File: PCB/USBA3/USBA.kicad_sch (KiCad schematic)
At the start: 22 parts, among them J1 USB_A, U1 ESP32-PICO-MINI-02, U2 Barcode, U3 CH340X, U4 QR, U5 MD8942

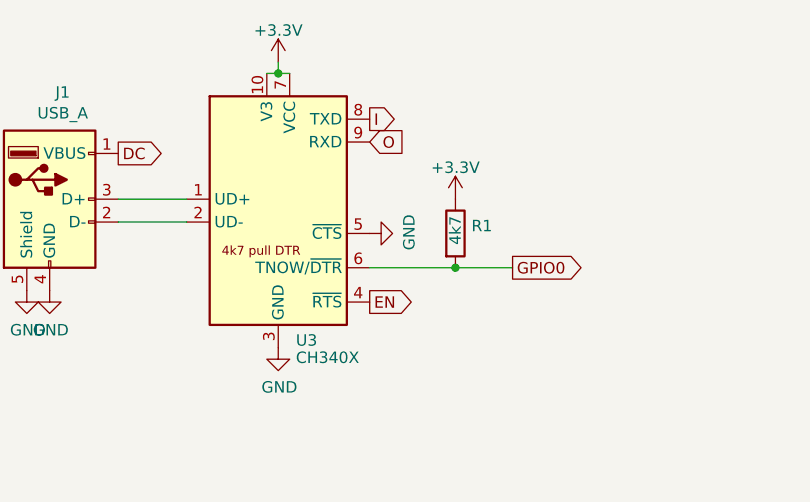
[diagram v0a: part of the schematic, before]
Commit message: Fix CH340X
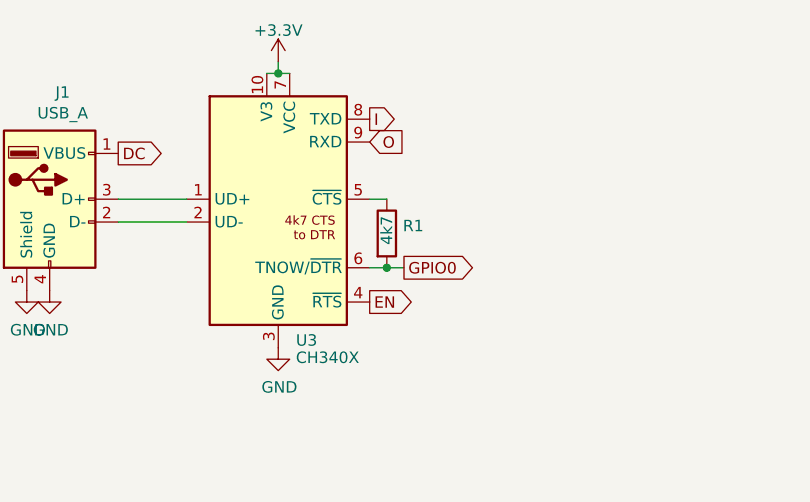
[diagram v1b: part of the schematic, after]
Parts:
- U3: JLCPCB Rotation Offset -90 -> 90
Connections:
- net +3.3V: no longer R1.1
- net GND: no longer U3.5 (~{CTS})
- new net: R1.1, U3.5 (~{CTS})
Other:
- moved on the sheet: R1
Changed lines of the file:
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@@
   (junction (at 193.04 43.18) (diameter 0) (color 0 0 0 0)
   )
-  (junction (at 212.725 64.77) (diameter 0) (color 0 0 0 0)
+  (junction (at 205.105 64.77) (diameter 0) (color 0 0 0 0)
   )
   (junction (at 78.74 49.53) (diameter 0) (color 0 0 0 0)
@@
     (stroke (width 0) (type default))
   )
-  (wire (pts (xy 203.2 64.77) (xy 212.725 64.77))
+  (wire (pts (xy 203.2 64.77) (xy 205.105 64.77))
     (stroke (width 0) (type default))
   )
@@
     (stroke (width 0) (type default))
   )
-  (wire (pts (xy 212.725 64.77) (xy 219.075 64.77))
+  (wire (pts (xy 205.105 64.77) (xy 207.01 64.77))
     (stroke (width 0) (type default))
   )
@@
   )
   (wire (pts (xy 193.04 41.91) (xy 193.04 43.18))
+    (stroke (width 0) (type default))
+  )
+  (wire (pts (xy 203.2 57.15) (xy 205.105 57.15))
     (stroke (width 0) (type default))
   )
@@
     )
   )
-  (global_label "GPIO0" (shape output) (at 219.075 64.77 0) (fields_autoplaced)
-    (effects (font (size 1.27 1.27)) (justify left))
-    (property "Intersheetrefs" "${INTERSHEET_REFS}" (at 227.0114 64.77 0)
+  (global_label "GPIO0" (shape output) (at 207.01 64.77 0) (fields_autoplaced)
+    (effects (font (size 1.27 1.27)) (justify left))
+    (property "Intersheetrefs" "${INTERSHEET_REFS}" (at 214.9464 64.77 0)
       (effects (font (size 1.27 1.27)) (justify left) hide)
     )
@@
       (effects (font (size 1.27 1.27)) hide)
     )
-    (property "JLCPCB Rotation Offset" "-90" (at 203.2 54.61 0)
+    (property "JLCPCB Rotation Offset" "90" (at 203.2 54.61 0)
       (effects (font (size 1.27 1.27)) hide)
     )
@@
     )
   )
-  (symbol (lib_id "Device:R") (at 212.725 60.96 0) (unit 1)
-    (in_bom yes) (on_board yes) (dnp no)
-    (property "Reference" "R1" (at 214.503 60.1253 0)
-      (effects (font (size 1.27 1.27)) (justify left))
-    )
-    (property "Value" "4k7" (at 212.725 62.23 90)
-      (effects (font (size 1.27 1.27)) (justify left))
-    )
-    (property "Footprint" "RevK:R_0402" (at 210.947 60.96 90)
-      (effects (font (size 1.27 1.27)) hide)
-    )
-    (property "Datasheet" "~" (at 212.725 60.96 0)
+  (symbol (lib_id "Device:R") (at 205.105 60.96 0) (unit 1)
+    (in_bom yes) (on_board yes) (dnp no)
+    (property "Reference" "R1" (at 206.883 60.1253 0)
+      (effects (font (size 1.27 1.27)) (justify left))
+    )
+    (property "Value" "4k7" (at 205.105 62.23 90)
+      (effects (font (size 1.27 1.27)) (justify left))
+    )
+    (property "Footprint" "RevK:R_0402" (at 203.327 60.96 90)
+      (effects (font (size 1.27 1.27)) hide)
+    )
+    (property "Datasheet" "~" (at 205.105 60.96 0)
       (effects (font (size 1.27 1.27)) hide)
     )
@@
     )
   )
-  (symbol (lib_id "power:GND") (at 203.2 60.96 90) (unit 1)
-    (in_bom yes) (on_board yes) (dnp no)
-    (property "Reference" "#PWR02" (at 209.55 60.96 0)
-      (effects (font (size 1.27 1.27)) hide)
-    )
-    (property "Value" "GND" (at 207.5942 60.833 0)
-      (effects (font (size 1.27 1.27)))
-    )
-    (property "Footprint" "" (at 203.2 60.96 0)
-      (effects (font (size 1.27 1.27)) hide)
-    )
-    (property "Datasheet" "" (at 203.2 60.96 0)
-      (effects (font (size 1.27 1.27)) hide)
-    )
-    (pin "1")
-    (instances
-      (project "USBA"
-        (path "/2d210a96-f81f-42a9-8bf4-1b43c11086f3"
-          (reference "#PWR02") (unit 1)
-        )
-      )
-    )
-  )
   (symbol (lib_id "RevK:PCB") (at 250.19 172.72 0) (unit 1)
     (in_bom no) (on_board yes) (dnp no)
@@
         )
       )
-    )
-  )
-  (symbol (lib_id "power:+3.3V") (at 212.725 57.15 0) (unit 1)
-    (in_bom yes) (on_board yes) (dnp no) (fields_autoplaced)
-    (property "Reference" "#PWR05" (at 212.725 60.96 0)
-      (effects (font (size 1.27 1.27)) hide)
-    )
-    (property "Value" "+3.3V" (at 212.725 53.6481 0)
-      (effects (font (size 1.27 1.27)))
-    )
-    (property "Footprint" "" (at 212.725 57.15 0)
-      (effects (font (size 1.27 1.27)) hide)
-    )
-    (property "Datasheet" "" (at 212.725 57.15 0)
-      (effects (font (size 1.27 1.27)) hide)
-    )
-    (pin "1")
-    (instances
-      (project "USBA"
-        (path "/2d210a96-f81f-42a9-8bf4-1b43c11086f3"
-          (reference "#PWR05") (unit 1)
-        )
-      )

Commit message: Tidy
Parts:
- removed C5: 1uF, RevK:C_0402, symbol Device:C
- removed R1: 4k7, RevK:R_0402, symbol Device:R
- removed R6: 10k, RevK:R_0402, symbol Device:R
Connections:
- net GPIO0: now also U3.5 (~{CTS})
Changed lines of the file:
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@@
   (junction (at 193.04 43.18) (diameter 0) (color 0 0 0 0)
   )
-  (junction (at 205.105 64.77) (diameter 0) (color 0 0 0 0)
-  )
-  (junction (at 78.74 49.53) (diameter 0) (color 0 0 0 0)
+  (junction (at 203.2 64.77) (diameter 0) (color 0 0 0 0)
   )
   (no_connect (at 121.92 80.01))
@@
     (stroke (width 0) (type default))
   )
-  (wire (pts (xy 203.2 64.77) (xy 205.105 64.77))
-    (stroke (width 0) (type default))
-  )
   (wire (pts (xy 121.92 58.42) (xy 124.46 58.42))
     (stroke (width 0) (type default))
   )
-  (wire (pts (xy 78.74 49.53) (xy 91.44 49.53))
-    (stroke (width 0) (type default))
-  )
-  (wire (pts (xy 72.39 49.53) (xy 78.74 49.53))
-    (stroke (width 0) (type default))
-  )
   (wire (pts (xy 191.77 43.18) (xy 193.04 43.18))
     (stroke (width 0) (type default))
   )
+  (wire (pts (xy 203.2 57.15) (xy 203.2 64.77))
+    (stroke (width 0) (type default))
+  )
   (wire (pts (xy 121.92 53.34) (xy 123.825 53.34))
     (stroke (width 0) (type default))
@@
     (stroke (width 0) (type default))
   )
-  (wire (pts (xy 205.105 64.77) (xy 207.01 64.77))
-    (stroke (width 0) (type default))
-  )
   (wire (pts (xy 175.26 57.15) (xy 182.88 57.15))
     (stroke (width 0) (type default))
@@
     (stroke (width 0) (type default))
   )
+  (wire (pts (xy 203.2 64.77) (xy 204.47 64.77))
+    (stroke (width 0) (type default))
+  )
   (wire (pts (xy 193.04 41.91) (xy 193.04 43.18))
-    (stroke (width 0) (type default))
-  )
-  (wire (pts (xy 203.2 57.15) (xy 205.105 57.15))
     (stroke (width 0) (type default))
   )
@@
     )
   )
-  (global_label "GPIO0" (shape output) (at 207.01 64.77 0) (fields_autoplaced)
-    (effects (font (size 1.27 1.27)) (justify left))
-    (property "Intersheetrefs" "${INTERSHEET_REFS}" (at 214.9464 64.77 0)
+  (global_label "GPIO0" (shape output) (at 204.47 64.77 0) (fields_autoplaced)
+    (effects (font (size 1.27 1.27)) (justify left))
+    (property "Intersheetrefs" "${INTERSHEET_REFS}" (at 212.4064 64.77 0)
       (effects (font (size 1.27 1.27)) (justify left) hide)
     )
@@
     )
   )
-  (global_label "EN" (shape input) (at 72.39 49.53 180) (fields_autoplaced)
+  (global_label "EN" (shape input) (at 91.44 49.53 180) (fields_autoplaced)
     (effects (font (size 1.27 1.27)) (justify right))
-    (property "Intersheetrefs" "${INTERSHEET_REFS}" (at 22.225 12.7 0)
+    (property "Intersheetrefs" "${INTERSHEET_REFS}" (at 41.275 12.7 0)
       (effects (font (size 1.27 1.27)) hide)
     )
@@
     )
   )
-  (symbol (lib_id "Device:R") (at 78.74 45.72 0) (unit 1)
-    (in_bom yes) (on_board yes) (dnp no)
-    (property "Reference" "R6" (at 80.518 44.8853 0)
-      (effects (font (size 1.27 1.27)) (justify left))
-    )
-    (property "Value" "10k" (at 78.74 46.99 90)
-      (effects (font (size 1.27 1.27)) (justify left))
-    )
-    (property "Footprint" "RevK:R_0402" (at 76.962 45.72 90)
-      (effects (font (size 1.27 1.27)) hide)
-    )
-    (property "Datasheet" "~" (at 78.74 45.72 0)
-      (effects (font (size 1.27 1.27)) hide)
-    )
-    (pin "1")
-    (pin "2")
-    (instances
-      (project "USBA"
-        (path "/2d210a96-f81f-42a9-8bf4-1b43c11086f3"
-          (reference "R6") (unit 1)
-        )
-      )
-    )
-  )
   (symbol (lib_id "power:GND") (at 193.04 73.66 0) (unit 1)
     (in_bom yes) (on_board yes) (dnp no)
@@
         (path "/2d210a96-f81f-42a9-8bf4-1b43c11086f3"
           (reference "#PWR01") (unit 1)
-        )
-      )
-    )
-  )
-  (symbol (lib_id "power:+3.3V") (at 78.74 41.91 0) (unit 1)
-    (in_bom yes) (on_board yes) (dnp no) (fields_autoplaced)
-    (property "Reference" "#PWR0103" (at 78.74 45.72 0)
-      (effects (font (size 1.27 1.27)) hide)
-    )
-    (property "Value" "+3.3V" (at 78.74 38.3342 0)
-      (effects (font (size 1.27 1.27)))
-    )
-    (property "Footprint" "" (at 78.74 41.91 0)
-      (effects (font (size 1.27 1.27)) hide)
-    )
-    (property "Datasheet" "" (at 78.74 41.91 0)
-      (effects (font (size 1.27 1.27)) hide)
-    )
-    (pin "1")
-    (instances
-      (project "USBA"
-        (path "/2d210a96-f81f-42a9-8bf4-1b43c11086f3"
-          (reference "#PWR0103") (unit 1)
         )
       )
@@
         (path "/2d210a96-f81f-42a9-8bf4-1b43c11086f3"
           (reference "#PWR0102") (unit 1)
-        )
-      )
-    )
-  )
-  (symbol (lib_id "Device:R") (at 205.105 60.96 0) (unit 1)
-    (in_bom yes) (on_board yes) (dnp no)
-    (property "Reference" "R1" (at 206.883 60.1253 0)
-      (effects (font (size 1.27 1.27)) (justify left))
-    )
-    (property "Value" "4k7" (at 205.105 62.23 90)
-      (effects (font (size 1.27 1.27)) (justify left))
-    )
-    (property "Footprint" "RevK:R_0402" (at 203.327 60.96 90)
-      (effects (font (size 1.27 1.27)) hide)
-    )
-    (property "Datasheet" "~" (at 205.105 60.96 0)
-      (effects (font (size 1.27 1.27)) hide)
-    )
-    (pin "1")
-    (pin "2")
-    (instances
-      (project "USBA"
-        (path "/2d210a96-f81f-42a9-8bf4-1b43c11086f3"
-          (reference "R1") (unit 1)
         )
       )
@@
     )
   )
-  (symbol (lib_id "Device:C") (at 78.74 53.34 180) (unit 1)
-    (in_bom yes) (on_board yes) (dnp no) (fields_autoplaced)
-    (property "Reference" "C5" (at 81.661 52.5053 0)
-      (effects (font (size 1.27 1.27)) (justify right))
-    )
-    (property "Value" "1uF" (at 81.661 55.0422 0)
-      (effects (font (size 1.27 1.27)) (justify right))
-    )
-    (property "Footprint" "RevK:C_0402" (at 77.7748 49.53 0)
-      (effects (font (size 1.27 1.27)) hide)
-    )
-    (property "Datasheet" "~" (at 78.74 53.34 0)
-      (effects (font (size 1.27 1.27)) hide)
-    )
-    (pin "1")
-    (pin "2")
-    (instances
-      (project "USBA"
-        (path "/2d210a96-f81f-42a9-8bf4-1b43c11086f3"
-          (reference "C5") (unit 1)
-        )
-      )
-    )
-  )
   (symbol (lib_id "Device:C") (at 133.985 127 0) (unit 1)
     (in_bom yes) (on_board yes) (dnp no) (fields_autoplaced)
@@
         )
       )
-    )
-  )
-  (symbol (lib_id "power:GND") (at 78.74 57.15 0) (unit 1)
-    (in_bom yes) (on_board yes) (dnp no) (fields_autoplaced)
-    (property "Reference" "#PWR0110" (at 78.74 63.5 0)
-      (effects (font (size 1.27 1.27)) hide)
-    )
-    (property "Value" "GND" (at 78.74 61.5934 0)
-      (effects (font (size 1.27 1.27)))
-    )
-    (property "Footprint" "" (at 78.74 57.15 0)
-      (effects (font (size 1.27 1.27)) hide)
-    )
-    (property "Datasheet" "" (at 78.74 57.15 0)
-      (effects (font (size 1.27 1.27)) hide)
-    )
-    (pin "1")
-    (instances
-      (project "USBA"
-        (path "/2d210a96-f81f-42a9-8bf4-1b43c11086f3"
-          (reference "#PWR0110") (unit 1)
-        )
-      )

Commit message: Added H.T
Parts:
- added U7: SHT40, RevK:Sensirion_DFN-4_1.5x1.5mm_P0.5mm_SHT4x, symbol RevK:SHT40
- D2: symbol Device:LED_RBGA -> Device:LED_RGBA
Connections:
- net +3.3V: now also U7.3 (VDD)
- net B: now also U1.33 (IO19); no longer U1.35 (IO21)
- net G: now also U1.35 (IO21); no longer U1.33 (IO19)
- net GND: now also U7.4 (VSS)
- net at D2.2 (GK): now also R5.1; no longer R7.1
- net at D2.3 (BK): now also R7.1; no longer R5.1
- net SDA: now reaches U1.26 (IO20)
- net SDA: now also U7.1 (SDA)
- net SCL: now reaches U1.27 (IO7)
- net SCL: now also U7.2 (SCL)
- no-connect marks 22 -> 20
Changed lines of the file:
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@@
   )
   (no_connect (at 121.92 80.01))
-  (no_connect (at 91.44 90.17))
   (no_connect (at 91.44 87.63))
   (no_connect (at 91.44 92.71))
@@
   (no_connect (at 91.44 62.23))
   (no_connect (at 91.44 64.77))
-  (no_connect (at 91.44 80.01))
   (no_connect (at 121.92 85.09))
   (no_connect (at 121.92 82.55))
@@
   (no_connect (at 91.44 85.09))
   (no_connect (at 91.44 57.15))
-  (no_connect (at 121.92 72.39))
+  (no_connect (at 91.44 90.17))
   (no_connect (at 91.44 72.39))
   (wire (pts (xy 121.92 63.5) (xy 124.46 63.5))
@@
     )
   )
-  (global_label "G" (shape output) (at 121.92 69.85 0) (fields_autoplaced)
+  (global_label "G" (shape output) (at 121.92 74.93 0) (fields_autoplaced)
     (effects (font (size 1.27 1.27)) (justify left))
-    (property "Intersheetrefs" "${INTERSHEET_REFS}" (at 41.275 -2.54 0)
+    (property "Intersheetrefs" "${INTERSHEET_REFS}" (at 41.275 2.54 0)
       (effects (font (size 1.27 1.27)) hide)
     )
@@
     )
   )
+  (global_label "SCL" (shape input) (at 161.29 95.25 180) (fields_autoplaced)
+    (effects (font (size 1.27 1.27)) (justify right))
+    (property "Intersheetrefs" "${INTERSHEET_REFS}" (at 155.4582 95.1706 0)
+      (effects (font (size 1.27 1.27)) (justify right) hide)
+    )
+  )
   (global_label "O" (shape output) (at 123.825 53.34 0) (fields_autoplaced)
     (effects (font (size 1.27 1.27)) (justify left))
@@
     )
   )
+  (global_label "SDA" (shape bidirectional) (at 161.29 100.33 180) (fields_autoplaced)
+    (effects (font (size 1.27 1.27)) (justify right))
+    (property "Intersheetrefs" "${INTERSHEET_REFS}" (at 155.3977 100.2506 0)
+      (effects (font (size 1.27 1.27)) (justify right) hide)
+    )
+  )
   (global_label "R" (shape input) (at 99.06 123.19 180) (fields_autoplaced)
     (effects (font (size 1.27 1.27)) (justify right))
@@
     )
   )
-  (global_label "B" (shape output) (at 121.92 74.93 0) (fields_autoplaced)
+  (global_label "SCL" (shape output) (at 91.44 80.01 180) (fields_autoplaced)
+    (effects (font (size 1.27 1.27)) (justify right))
+    (property "Intersheetrefs" "${INTERSHEET_REFS}" (at 85.6808 80.01 0)
+      (effects (font (size 1.27 1.27)) (justify right) hide)
+    )
+  )
+  (global_label "B" (shape output) (at 121.92 69.85 0) (fields_autoplaced)
     (effects (font (size 1.27 1.27)) (justify left))
-    (property "Intersheetrefs" "${INTERSHEET_REFS}" (at 41.275 0 0)
+    (property "Intersheetrefs" "${INTERSHEET_REFS}" (at 41.275 -5.08 0)
       (effects (font (size 1.27 1.27)) hide)
     )
@@
     (property "Intersheetrefs" "${INTERSHEET_REFS}" (at -3.81 27.94 0)
       (effects (font (size 1.27 1.27)) hide)
+    )
+  )
+  (global_label "SDA" (shape bidirectional) (at 121.92 72.39 0) (fields_autoplaced)
+    (effects (font (size 1.27 1.27)) (justify left))
+    (property "Intersheetrefs" "${INTERSHEET_REFS}" (at 128.6922 72.39 0)
+      (effects (font (size 1.27 1.27)) (justify left) hide)
     )
   )
@@
     )
   )
+  (symbol (lib_id "RevK:SHT40") (at 168.91 97.79 0) (unit 1)
+    (in_bom yes) (on_board yes) (dnp no) (fields_autoplaced)
+    (property "Reference" "U7" (at 174.752 96.9553 0)
+      (effects (font (size 1.27 1.27)) (justify left))
+    )
+    (property "Value" "SHT40" (at 174.752 99.4922 0)
+      (effects (font (size 1.27 1.27)) (justify left) hide)
+    )
+    (property "Footprint" "RevK:Sensirion_DFN-4_1.5x1.5mm_P0.5mm_SHT4x" (at 172.72 104.14 0)
+      (effects (font (size 1.27 1.27)) (justify left) hide)
+    )
+    (property "Datasheet" "https://sensirion.com/media/documents/33FD6951/624C4357/Datasheet_SHT4x.pdf" (at 172.72 106.68 0)
+      (effects (font (size 1.27 1.27)) (justify left) hide)
+    )
+    (property "LCSC Part #" "C2909890" (at 174.752 100.7607 0)
+      (effects (font (size 1.27 1.27)) (justify left) hide)
+    )
+    (pin "1")
+    (pin "2")
+    (pin "3")
+    (pin "4")
+    (instances
+      (project "EnvMon2"
+        (path "/12422a89-3d0c-485c-9386-f77121fd68fd"
+          (reference "U7") (unit 1)
+        )
+      )
+      (project "USBA"
+        (path "/2d210a96-f81f-42a9-8bf4-1b43c11086f3"
+          (reference "U6") (unit 1)
+        )
+      )
+    )
+  )
   (symbol (lib_id "RevK:Hidden") (at 198.12 121.285 0) (unit 1)
     (in_bom yes) (on_board yes) (dnp no)
@@
     )
   )
-  (symbol (lib_id "Device:LED_RBGA") (at 111.76 128.27 0) (unit 1)
+  (symbol (lib_id "Device:LED_RGBA") (at 111.76 128.27 0) (unit 1)
     (in_bom yes) (on_board yes) (dnp no)
     (property "Reference" "D2" (at 111.76 115.6462 0)
@@
     )
   )
+  (symbol (lib_id "power:GND") (at 171.45 105.41 0) (unit 1)
+    (in_bom yes) (on_board yes) (dnp no)
+    (property "Reference" "#PWR0110" (at 171.45 111.76 0)
+      (effects (font (size 1.27 1.27)) hide)
+    )
+    (property "Value" "GND" (at 171.45 109.8534 0)
+      (effects (font (size 1.27 1.27)))
+    )
+    (property "Footprint" "" (at 171.45 105.41 0)
+      (effects (font (size 1.27 1.27)) hide)
+    )
+    (property "Datasheet" "" (at 171.45 105.41 0)
+      (effects (font (size 1.27 1.27)) hide)
+    )
+    (pin "1")
+    (instances
+      (project "EnvMon2"
+        (path "/12422a89-3d0c-485c-9386-f77121fd68fd"
+          (reference "#PWR0110") (unit 1)
+        )
+      )
+      (project "USBA"
+        (path "/2d210a96-f81f-42a9-8bf4-1b43c11086f3"
+          (reference "#PWR05") (unit 1)
+        )
+      )
+    )
+  )
   (symbol (lib_id "power:GND") (at 133.985 130.81 0) (unit 1)
     (in_bom yes) (on_board yes) (dnp no) (fields_autoplaced)
@@
         )
       )
+    )
+  )
+  (symbol (lib_id "power:+3.3V") (at 171.45 90.17 0) (unit 1)
+    (in_bom yes) (on_board yes) (dnp no)
+    (property "Reference" "#PWR0111" (at 171.45 93.98 0)
+      (effects (font (size 1.27 1.27)) hide)
+    )
+    (property "Value" "+3.3V" (at 172.847 89.3338 0)
+      (effects (font (size 1.27 1.27)) (justify left))
+    )
+    (property "Footprint" "" (at 171.45 90.17 0)
+      (effects (font (size 1.27 1.27)) hide)
+    )
+    (property "Datasheet" "" (at 171.45 90.17 0)
+      (effects (font (size 1.27 1.27)) hide)
+    )
+    (pin "1")
+    (instances
+      (project "EnvMon2"
+        (path "/12422a89-3d0c-485c-9386-f77121fd68fd"
+          (reference "#PWR0111") (unit 1)
+        )
+      )
+      (project "USBA"
+        (path "/2d210a96-f81f-42a9-8bf4-1b43c11086f3"
+          (reference "#PWR02") (unit 1)
+        )
+      )

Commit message: Order
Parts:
- U3: JLCPCB Rotation Offset 90 -> -90
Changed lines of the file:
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@@
       (effects (font (size 1.27 1.27)) hide)
     )
-    (property "JLCPCB Rotation Offset" "90" (at 203.2 54.61 0)
+    (property "JLCPCB Rotation Offset" "-90" (at 203.2 54.61 0)
       (effects (font (size 1.27 1.27)) hide)
     )

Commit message: Tweak
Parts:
- R10: value 40k2 -> 39k2
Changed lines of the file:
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@@
       (effects (font (size 1.27 1.27)))
     )
-    (property "Value" "40k2" (at 204.47 128.905 90)
+    (property "Value" "39k2" (at 204.47 128.905 90)
       (effects (font (size 1.27 1.27)) (justify left))
     )
